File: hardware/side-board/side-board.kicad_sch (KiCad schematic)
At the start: 25 parts, among them IC101 TPS62933DRLR, IC102 NUP2105LT1G, J101 Inter-board Connector

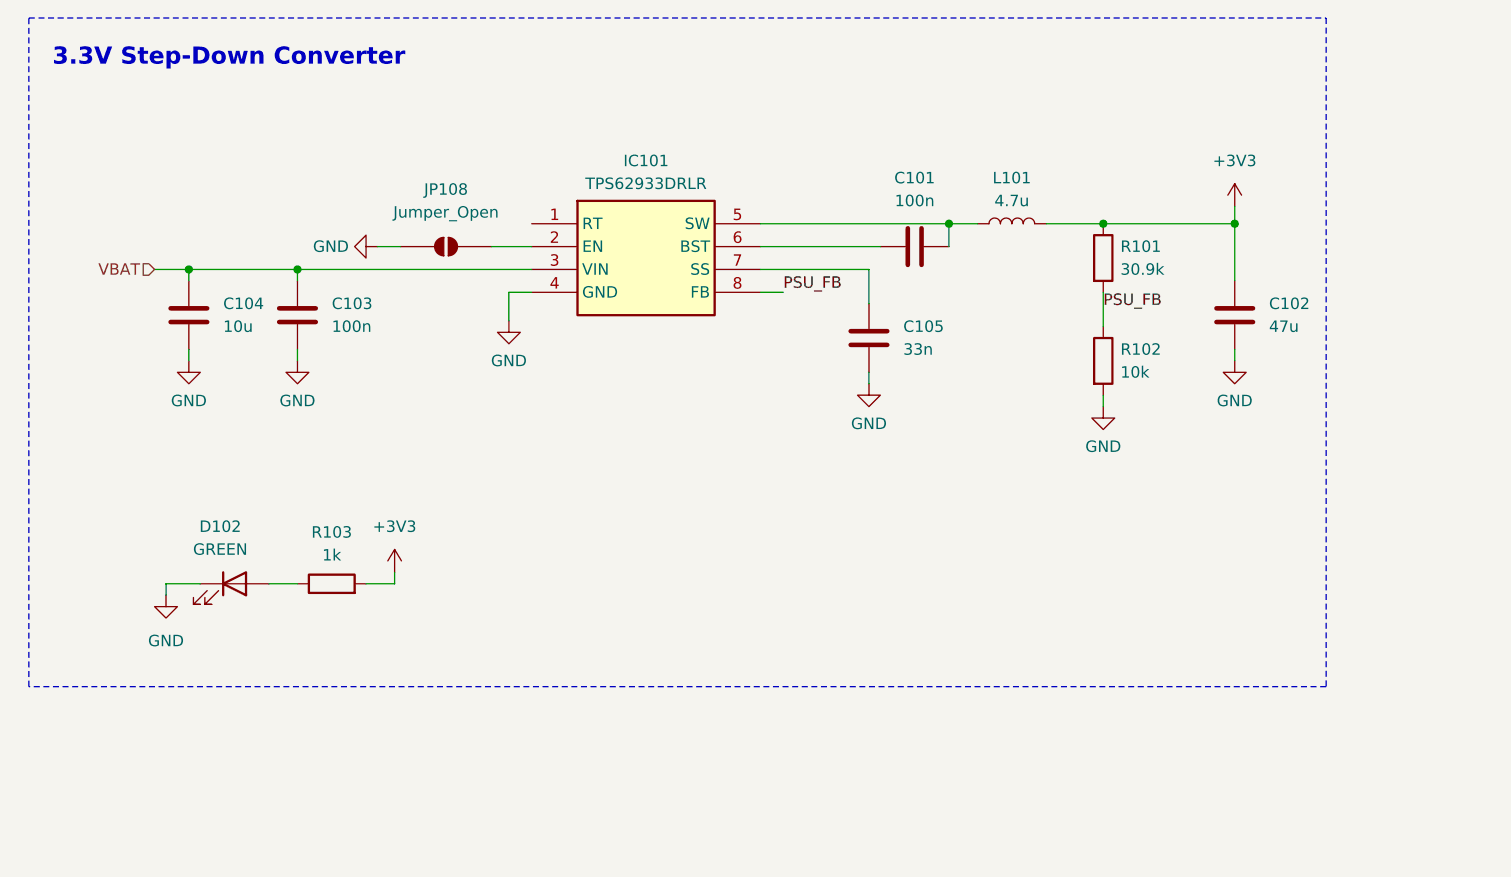
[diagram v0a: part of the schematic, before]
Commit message: Added more ICs for power board
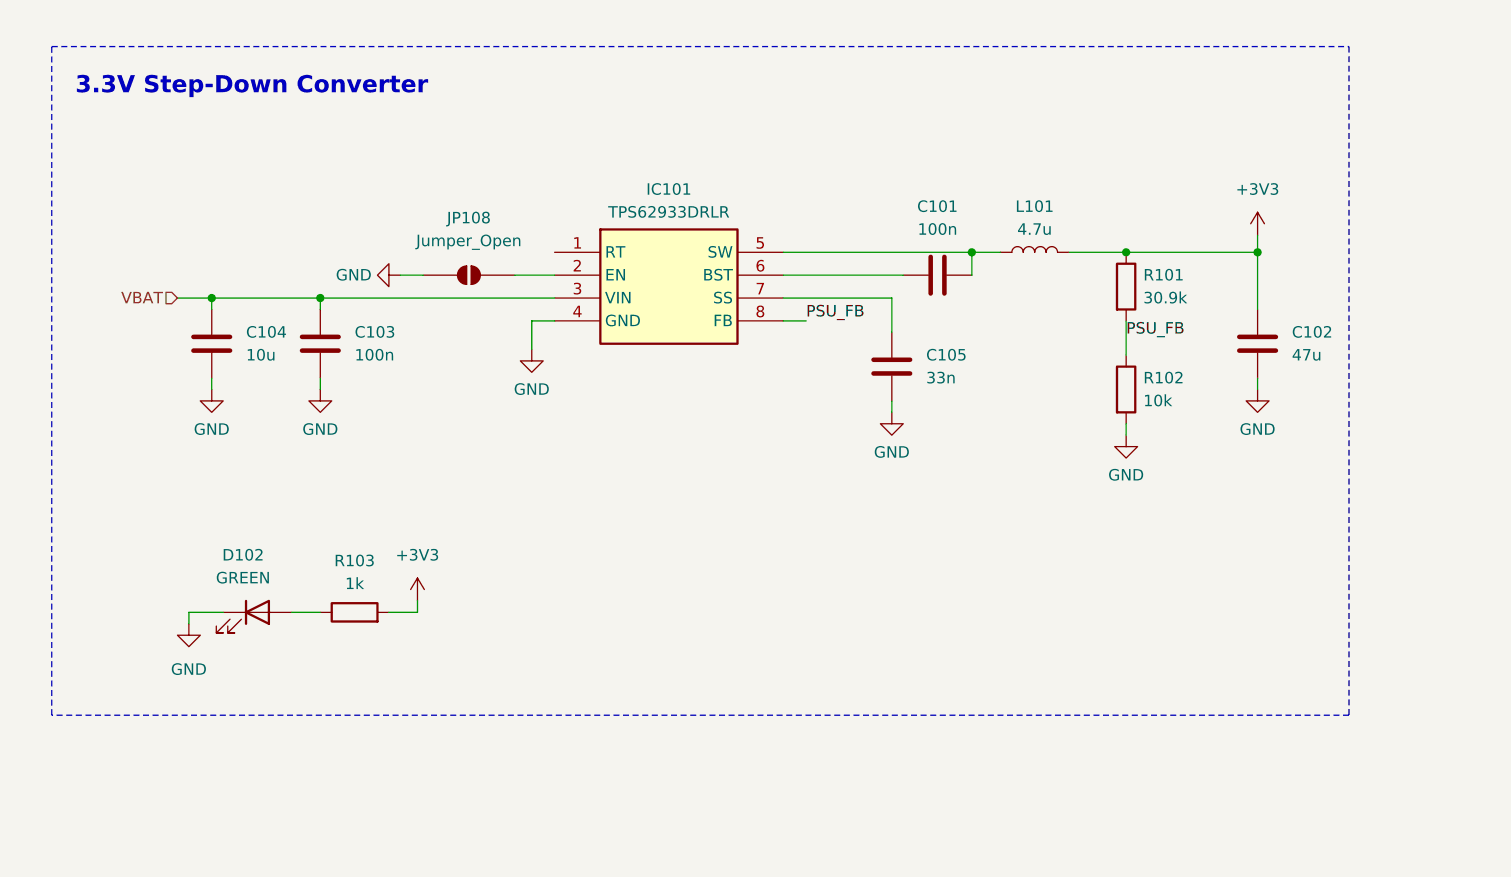
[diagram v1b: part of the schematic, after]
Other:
- moved on the sheet: C101, C102, C103, C104, C105, D102, IC101, JP108, L101, R101, R102, R103

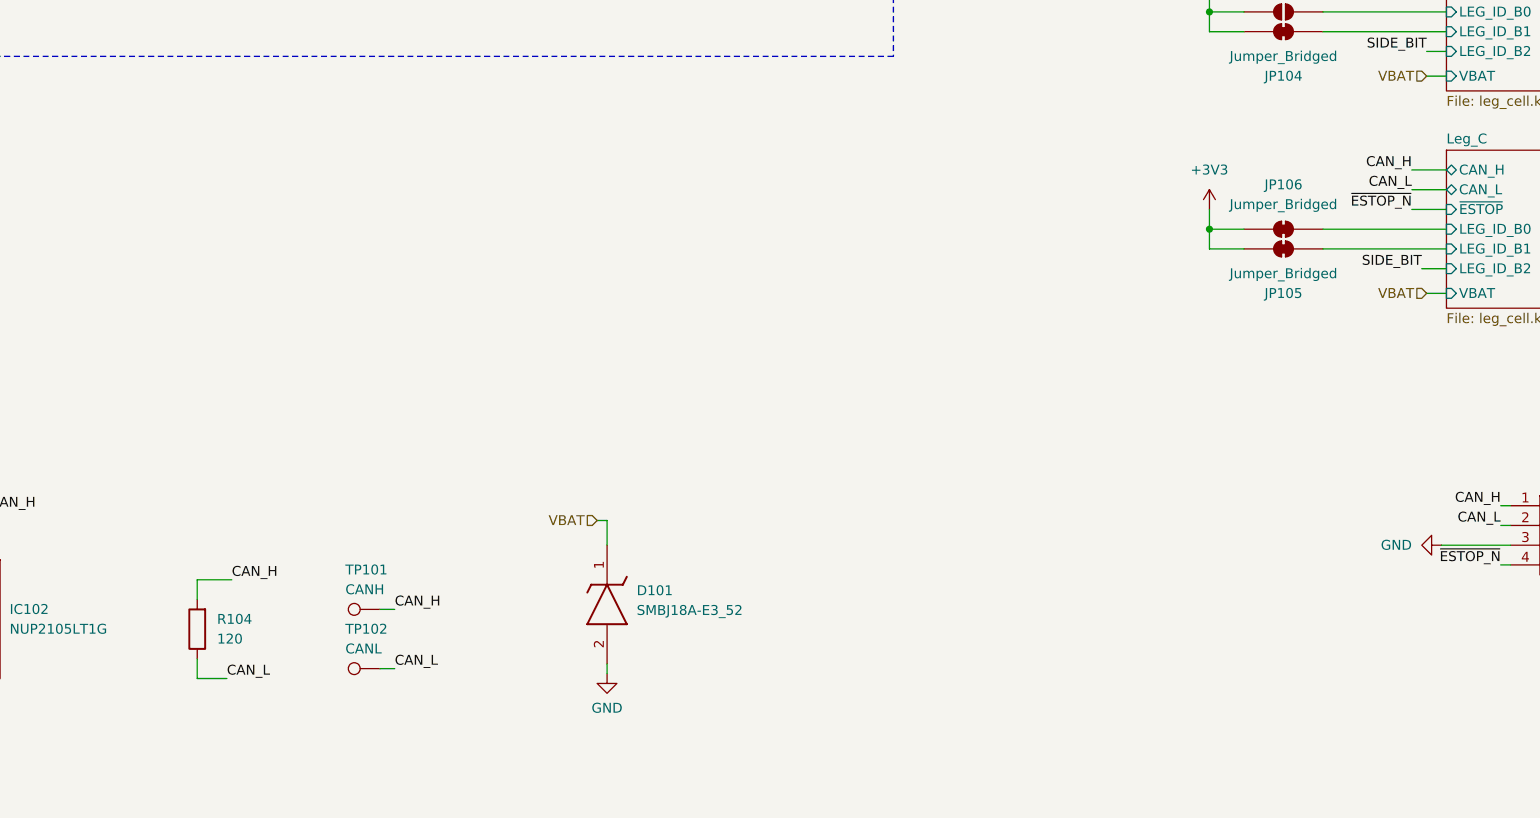
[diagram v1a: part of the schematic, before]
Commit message: add side board e-stop diode, cell fuse and connectors
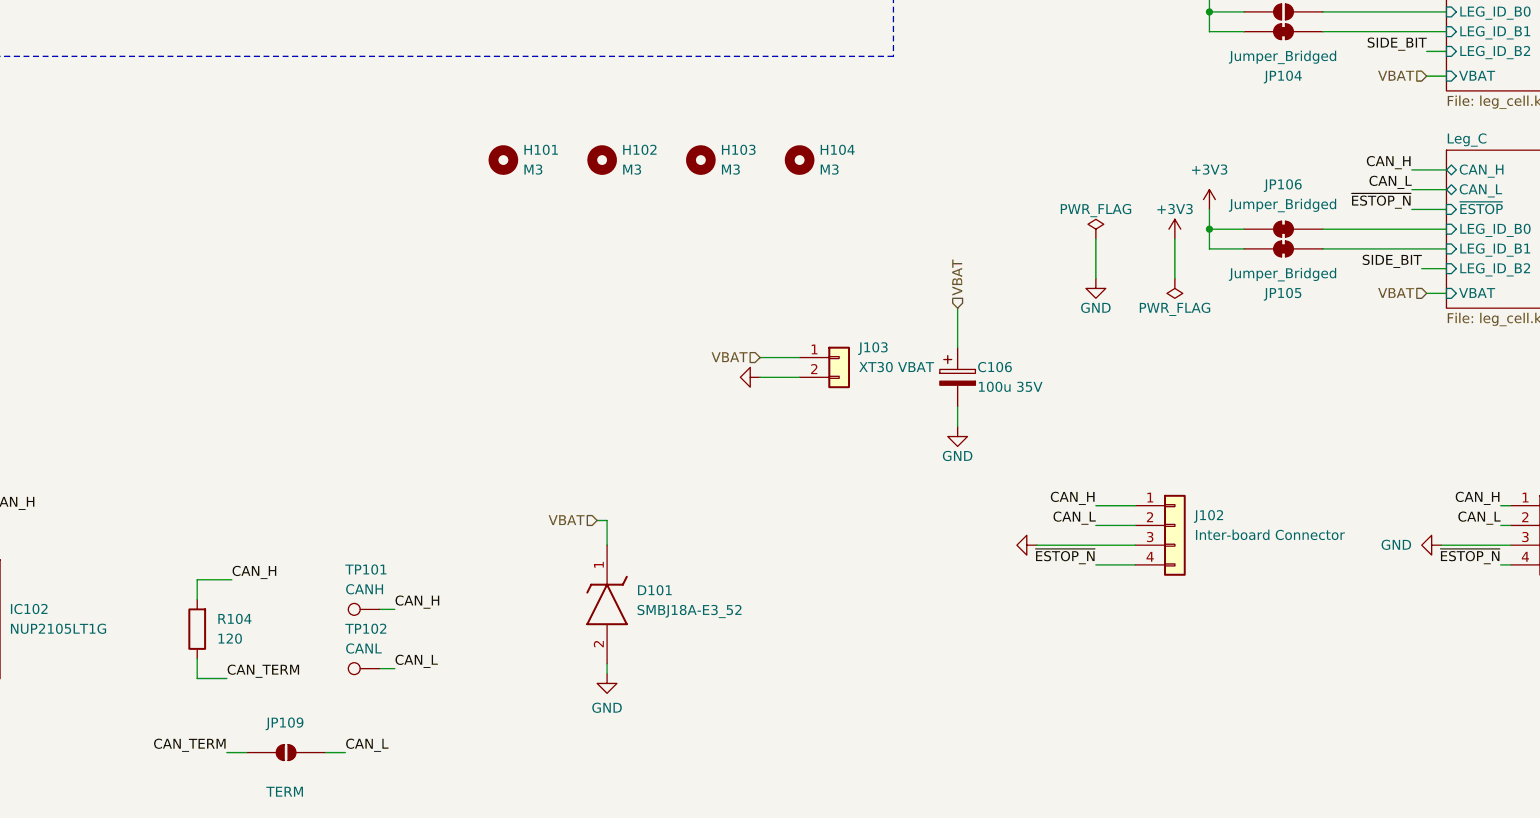
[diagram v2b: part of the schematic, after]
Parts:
- added C106: 100u 35V, Capacitor_SMD:CP_Elec_8x10.5, symbol Device:C_Polarized
- added H101, H102, H103, H104: M3, MountingHole:MountingHole_3.2mm_M3, symbol Mechanical:MountingHole
- added J102: Inter-board Connector, Connector_JST:JST_GH_SM04B-GHS-TB_1x04-1MP_P1.25mm_Horizontal, symbol Connector_Generic:Conn_01x04
- added J103: XT30 VBAT, Connector_AMASS:AMASS_XT30PW-M_1x02_P2.50mm_Horizontal, symbol Connector_Generic:Conn_01x02
- added JP109: TERM, Jumper:SolderJumper-2_P1.3mm_Open_Pad1.0x1.5mm, symbol Jumper:SolderJumper_2_Open
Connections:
- net CAN_H: now also J102.1 (Pin_1)
- net CAN_L: now also J102.2 (Pin_2), JP109.2 (B); no longer R104.1
- net GND: now also C106.2, J102.3 (Pin_3), J103.2 (Pin_2)
- net VBAT: now also C106.1, J103.1 (Pin_1)
- net ~{ESTOP_N}: now also J102.4 (Pin_4)
- new net CAN_TERM: JP109.1 (A), R104.1

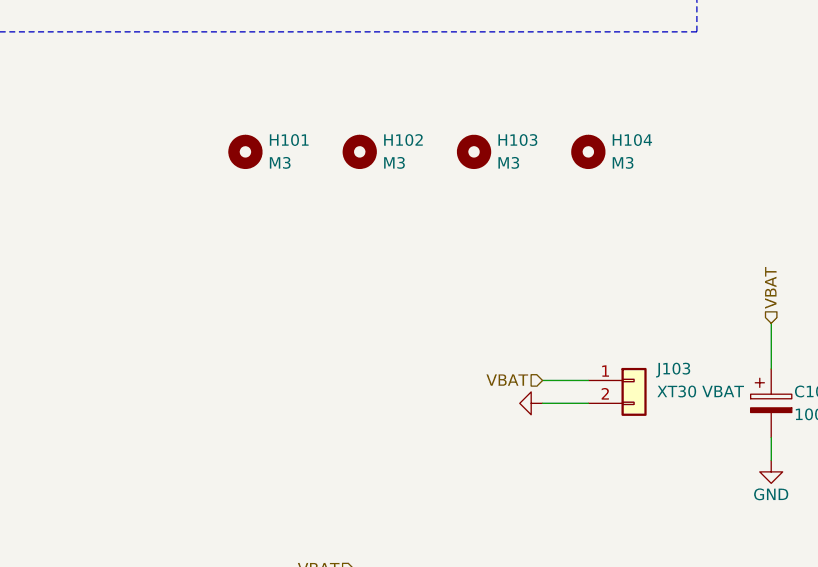
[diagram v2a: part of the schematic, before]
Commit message: side board: 1206 cell fuse, test points
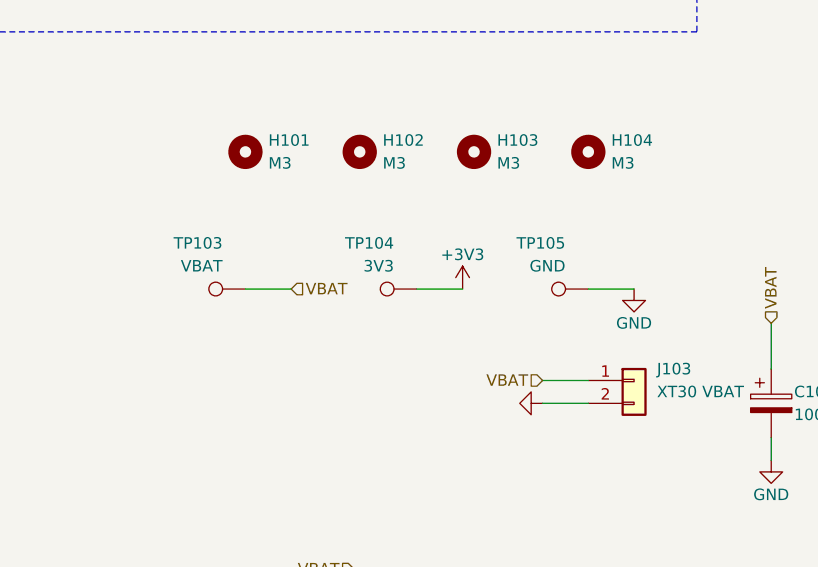
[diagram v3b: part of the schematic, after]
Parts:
- added TP103: VBAT, TestPoint:TestPoint_Pad_D2.0mm, symbol Connector:TestPoint
- added TP104: 3V3, TestPoint:TestPoint_Pad_D2.0mm, symbol Connector:TestPoint
- added TP105: GND, TestPoint:TestPoint_Pad_D2.0mm, symbol Connector:TestPoint
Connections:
- net +3V3: now also TP104.1
- net GND: now also TP105.1
- net VBAT: now also TP103.1

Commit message: side board: amrm inductors, 1206 buck input cap, xh can connector, rt no-connect
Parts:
- J102: footprint Connector_JST:JST_GH_SM04B-GHS-TB_1x04-1MP_P1.25mm_Horizontal -> Connector_JST:JST_XH_S4B-XH-A-1_1x04_P2.50mm_Horizontal
- L101: footprint (none) -> vector:INDPM116102X400N; Manufacturer_Part_Number (none) -> AMRM001010404R7MA1
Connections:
- no-connect marks 0 -> 1

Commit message: Updated PCB of side-board
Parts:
- J101, J102: footprint Connector_JST:JST_XH_S4B-XH-A-1_1x04_P2.50mm_Horizontal -> Connector_JST:JST_XH_B4B-XH-A_1x04_P2.50mm_Vertical
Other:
- moved on the sheet: C106, H101, H102, H103, H104, J103, JP101, JP102, JP103, JP104, JP105, JP106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

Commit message: Updated sideboard PCB
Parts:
- C101, C103, C104, C105: footprint Capacitor_SMD:C_0805_2012Metric -> Capacitor_SMD:C_0603_1608Metric
- H101, H102, H103, H104: footprint MountingHole:MountingHole_3.2mm_M3 -> MountingHole:MountingHole_3.2mm_M3_DIN965_Pad_TopBottom
- J103: footprint Connector_AMASS:AMASS_XT30PW-M_1x02_P2.50mm_Horizontal -> Connector_AMASS:AMASS_XT30U-M_1x02_P5.0mm_Vertical
- L101: footprint vector:INDPM116102X400N -> vector:INDPM4441X200N; Manufacturer_Part_Number AMRM001010404R7MA1 -> SRP4020TA-4R7M
- R101, R102: footprint Resistor_SMD:R_0805_2012Metric -> Resistor_SMD:R_0603_1608Metric
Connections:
- net SW: now reaches C101.2, IC101.5 (SW), L101.1
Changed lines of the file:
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@@
 		)
 	)
+	(label "SW"
+		(at 122.555 41.91 0)
+		(effects
+			(font
+				(size 1.27 1.27)
+			)
+			(justify left bottom)
+		)
+	)
 	(label "SIDE_BIT"
 		(at 229.235 31.75 0)
@@
 			)
 		)
-		(property "Footprint" "Resistor_SMD:R_0805_2012Metric"
+		(property "Footprint" "Resistor_SMD:R_0603_1608Metric"
 			(at 137.922 57.15 90)
 			(hide yes)
@@
 			)
 		)
-		(property "Footprint" "Capacitor_SMD:C_0805_2012Metric"
+		(property "Footprint" "Capacitor_SMD:C_0603_1608Metric"
 			(at 37.1348 48.26 0)
 			(hide yes)
@@
 			)
 		)
-		(property "Footprint" "MountingHole:MountingHole_3.2mm_M3"
+		(property "Footprint" "MountingHole:MountingHole_3.2mm_M3_DIN965_Pad_TopBottom"
 			(at 78.74 102.235 0)
 			(hide yes)
@@
 			)
 		)
-		(property "Footprint" "Connector_AMASS:AMASS_XT30PW-M_1x02_P2.50mm_Horizontal"
+		(property "Footprint" "Connector_AMASS:AMASS_XT30U-M_1x02_P5.0mm_Vertical"
 			(at 133.985 123.825 0)
 			(hide yes)
@@
 			)
 		)
-		(property "Footprint" "Capacitor_SMD:C_0805_2012Metric"
+		(property "Footprint" "Capacitor_SMD:C_0603_1608Metric"
 			(at 122.555 43.4848 0)
 			(hide yes)
@@
 			)
 		)
-		(property "Footprint" "MountingHole:MountingHole_3.2mm_M3"
+		(property "Footprint" "MountingHole:MountingHole_3.2mm_M3_DIN965_Pad_TopBottom"
 			(at 66.04 102.235 0)
 			(hide yes)
@@
 			)
 		)
-		(property "Footprint" "vector:INDPM116102X400N"
+		(property "Footprint" "vector:INDPM4441X200N"
 			(at 129.54 41.91 0)
 			(hide yes)
@@
 			)
 		)
-		(property "Manufacturer_Part_Number" "AMRM001010404R7MA1"
+		(property "Manufacturer_Part_Number" "SRP4020TA-4R7M"
 			(at 129.54 41.91 0)
 			(hide yes)
@@
 			)
 		)
-		(property "Footprint" "Capacitor_SMD:C_0805_2012Metric"
+		(property "Footprint" "Capacitor_SMD:C_0603_1608Metric"
 			(at 49.1998 48.26 0)
 			(hide yes)
@@
 			)
 		)
-		(property "Footprint" "MountingHole:MountingHole_3.2mm_M3"
+		(property "Footprint" "MountingHole:MountingHole_3.2mm_M3_DIN965_Pad_TopBottom"
 			(at 53.34 102.235 0)
 			(hide yes)
@@
 			)
 		)
-		(property "Footprint" "Resistor_SMD:R_0805_2012Metric"
+		(property "Footprint" "Resistor_SMD:R_0603_1608Metric"
 			(at 137.922 45.72 90)
 			(hide yes)
@@
 			)
 		)
-		(property "Footprint" "Capacitor_SMD:C_0805_2012Metric"
+		(property "Footprint" "Capacitor_SMD:C_0603_1608Metric"
 			(at 112.6998 50.8 0)
 			(hide yes)
@@
 			)
 		)
-		(property "Footprint" "MountingHole:MountingHole_3.2mm_M3"
+		(property "Footprint" "MountingHole:MountingHole_3.2mm_M3_DIN965_Pad_TopBottom"
 			(at 40.64 102.235 0)
 			(hide yes)

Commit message: Updated PCB placement sideboard
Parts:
- JP107: value Jumper_Open -> SIDE_BIT
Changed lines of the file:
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@@
 	(wire
 		(pts
-			(xy 195.58 156.21) (xy 182.88 156.21)
+			(xy 195.58 156.21) (xy 186.055 156.21)
 		)
 		(stroke
@@
 	(wire
 		(pts
-			(xy 195.58 153.67) (xy 190.5 153.67)
+			(xy 195.58 153.67) (xy 194.31 153.67)
 		)
 		(stroke
@@
 	(wire
 		(pts
-			(xy 195.58 158.75) (xy 190.5 158.75)
+			(xy 195.58 158.75) (xy 194.31 158.75)
 		)
 		(stroke
@@
 	(wire
 		(pts
-			(xy 195.58 151.13) (xy 190.5 151.13)
+			(xy 195.58 151.13) (xy 194.31 151.13)
 		)
 		(stroke
@@
 	(wire
 		(pts
-			(xy 234.95 156.21) (xy 243.84 156.21)
+			(xy 234.315 156.21) (xy 243.84 156.21)
 		)
 		(stroke
@@
 	)
 	(label "CAN_L"
-		(at 190.5 153.67 180)
+		(at 194.31 153.67 180)
 		(effects
 			(font
@@
 	)
 	(label "~{ESTOP_N}"
-		(at 190.5 158.75 180)
+		(at 194.31 158.75 180)
 		(effects
 			(font
@@
 	)
 	(label "CAN_H"
-		(at 190.5 151.13 180)
+		(at 194.31 151.13 180)
 		(effects
 			(font
@@
 	(symbol
 		(lib_id "power:GND")
-		(at 182.88 156.21 270)
+		(at 186.055 156.21 270)
 		(unit 1)
 		(body_style 1)
@@
 		(dnp no)
 		(property "Reference" "#PWR501"
-			(at 182.88 162.56 0)
+			(at 186.055 162.56 0)
 			(hide yes)
 			(show_name no)
@@
 		)
 		(property "Value" "GND"
-			(at 182.88 160.02 0)
-			(hide yes)
+			(at 180.975 156.21 90)
 			(show_name no)
 			(do_not_autoplace no)
@@
 		)
 		(property "Footprint" ""
-			(at 182.88 156.21 0)
+			(at 186.055 156.21 0)
 			(show_name no)
 			(do_not_autoplace no)
@@
 		)
 		(property "Datasheet" ""
-			(at 182.88 156.21 0)
+			(at 186.055 156.21 0)
 			(show_name no)
 			(do_not_autoplace no)
@@
 		)
 		(property "Description" ""
-			(at 182.88 156.21 0)
+			(at 186.055 156.21 0)
 			(show_name no)
 			(do_not_autoplace no)
@@
 	(symbol
 		(lib_id "power:GND")
-		(at 234.95 156.21 270)
+		(at 234.315 156.21 270)
 		(unit 1)
 		(body_style 1)
@@
 		(fields_autoplaced yes)
 		(property "Reference" "#PWR0113"
-			(at 228.6 156.21 0)
+			(at 227.965 156.21 0)
 			(hide yes)
 			(show_name no)
@@
 		)
 		(property "Value" "GND"
-			(at 231.14 156.2099 90)
+			(at 230.505 156.2099 90)
 			(show_name no)
 			(do_not_autoplace no)
@@
 		)
 		(property "Footprint" ""
-			(at 234.95 156.21 0)
+			(at 234.315 156.21 0)
 			(hide yes)
 			(show_name no)
@@
 		)
 		(property "Datasheet" ""
-			(at 234.95 156.21 0)
+			(at 234.315 156.21 0)
 			(hide yes)
 			(show_name no)
@@
 		)
 		(property "Description" "Power symbol creates a global label with name \"GND\" , ground"
-			(at 234.95 156.21 0)
+			(at 234.315 156.21 0)
 			(hide yes)
 			(show_name no)
@@
 			)
 		)
-		(property "Value" "Jumper_Open"
+		(property "Value" "SIDE_BIT"
 			(at 220.345 27.94 0)
 			(show_name no)

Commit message: Compacted side board pcb
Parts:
- added J104: SWD PWR, Connector_PinHeader_2.54mm:PinHeader_1x02_P2.54mm_Vertical, symbol Connector_Generic:Conn_01x02
- C101, C105: footprint Capacitor_SMD:C_0603_1608Metric -> Capacitor_SMD:C_0402_1005Metric
- C103: value 100n -> 100n 50V; footprint Capacitor_SMD:C_0603_1608Metric -> Capacitor_SMD:C_0402_1005Metric
- R101, R102, R103, R104: footprint Resistor_SMD:R_0603_1608Metric -> Resistor_SMD:R_0402_1005Metric
- TP101, TP102, TP103, TP104, TP105: footprint TestPoint:TestPoint_Pad_D2.0mm -> TestPoint:TestPoint_Pad_D1.0mm
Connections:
- net +3V3: now also J104.1 (Pin_1)
- net GND: now also J104.2 (Pin_2)
